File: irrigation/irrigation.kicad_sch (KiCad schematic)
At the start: 28 parts, among them J1 Power, J2 Power, J3 Power, J4 Power, J5 Power, J6 Power, J7 24V Jmp, J8 0V Jmp, K1 PLC-RPT-24DC/21, K3 PLC-RPT-24DC/21, M1 Pump, SW1 25% Full, SW2 50% Full, SW3 75% Full, SW4 100% Full, SW5 Well Empty, U1 MPPT-Charger

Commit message: More labels
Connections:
- net 8: now reaches K1.11, K3.14
- no-connect marks 0 -> 12
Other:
- note removed: "Need connectors for charge controller"
- moved on the sheet: BT1, BT2, SC1, SC2

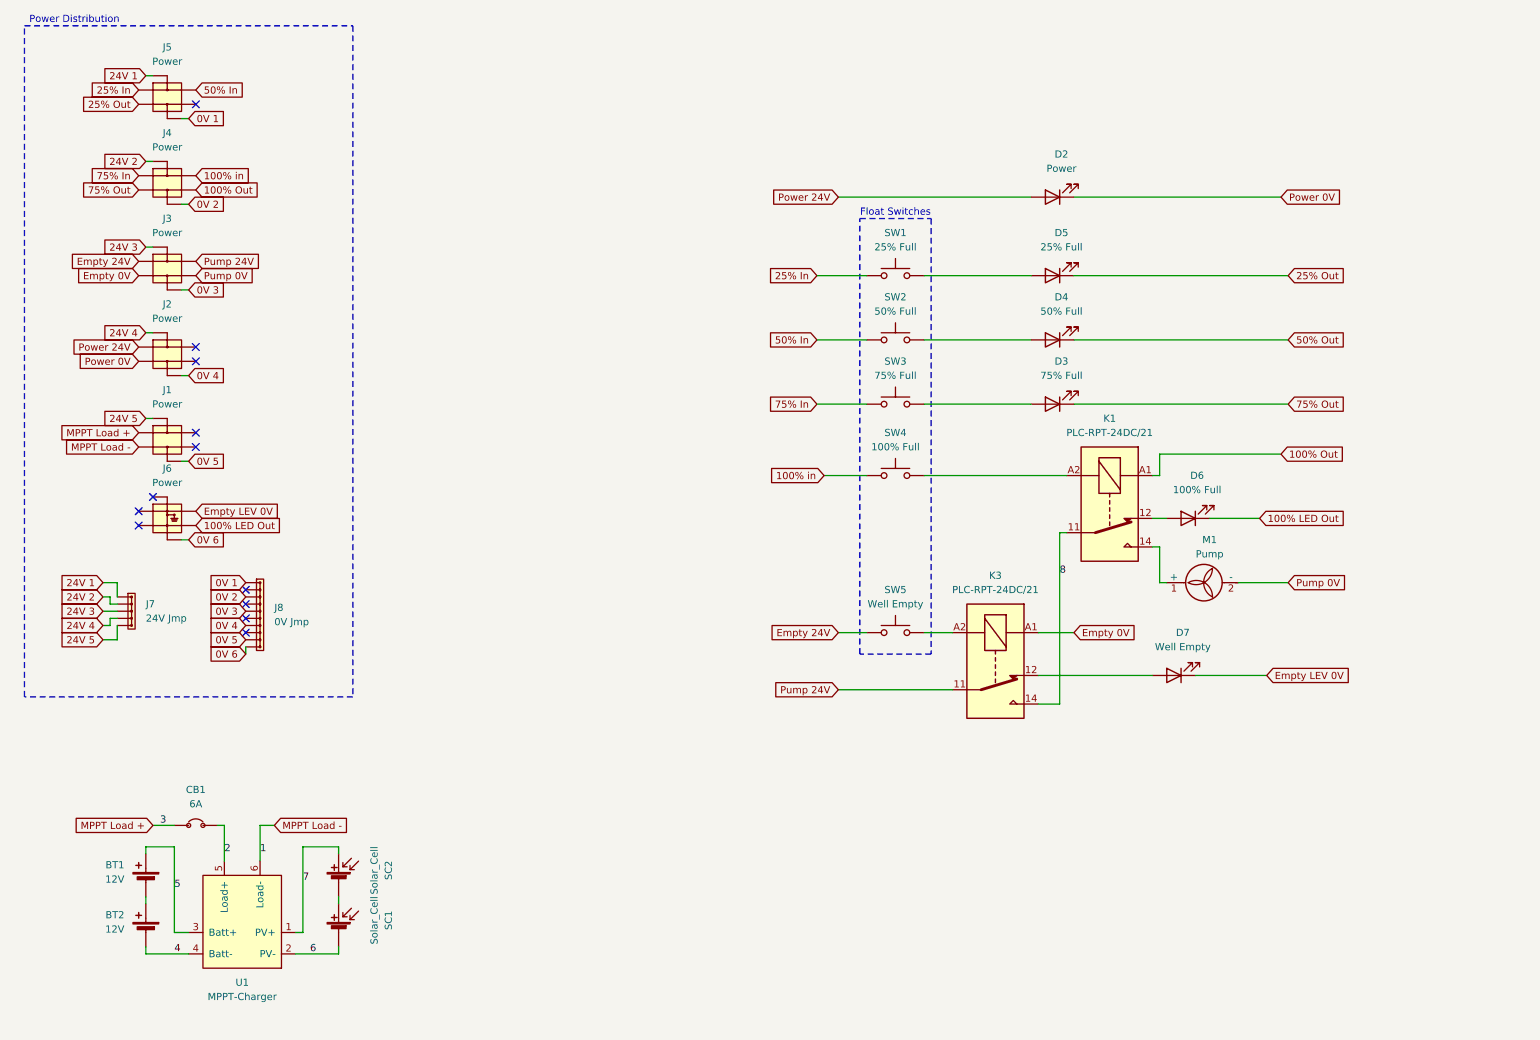
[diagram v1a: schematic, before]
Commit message: All wires labeled
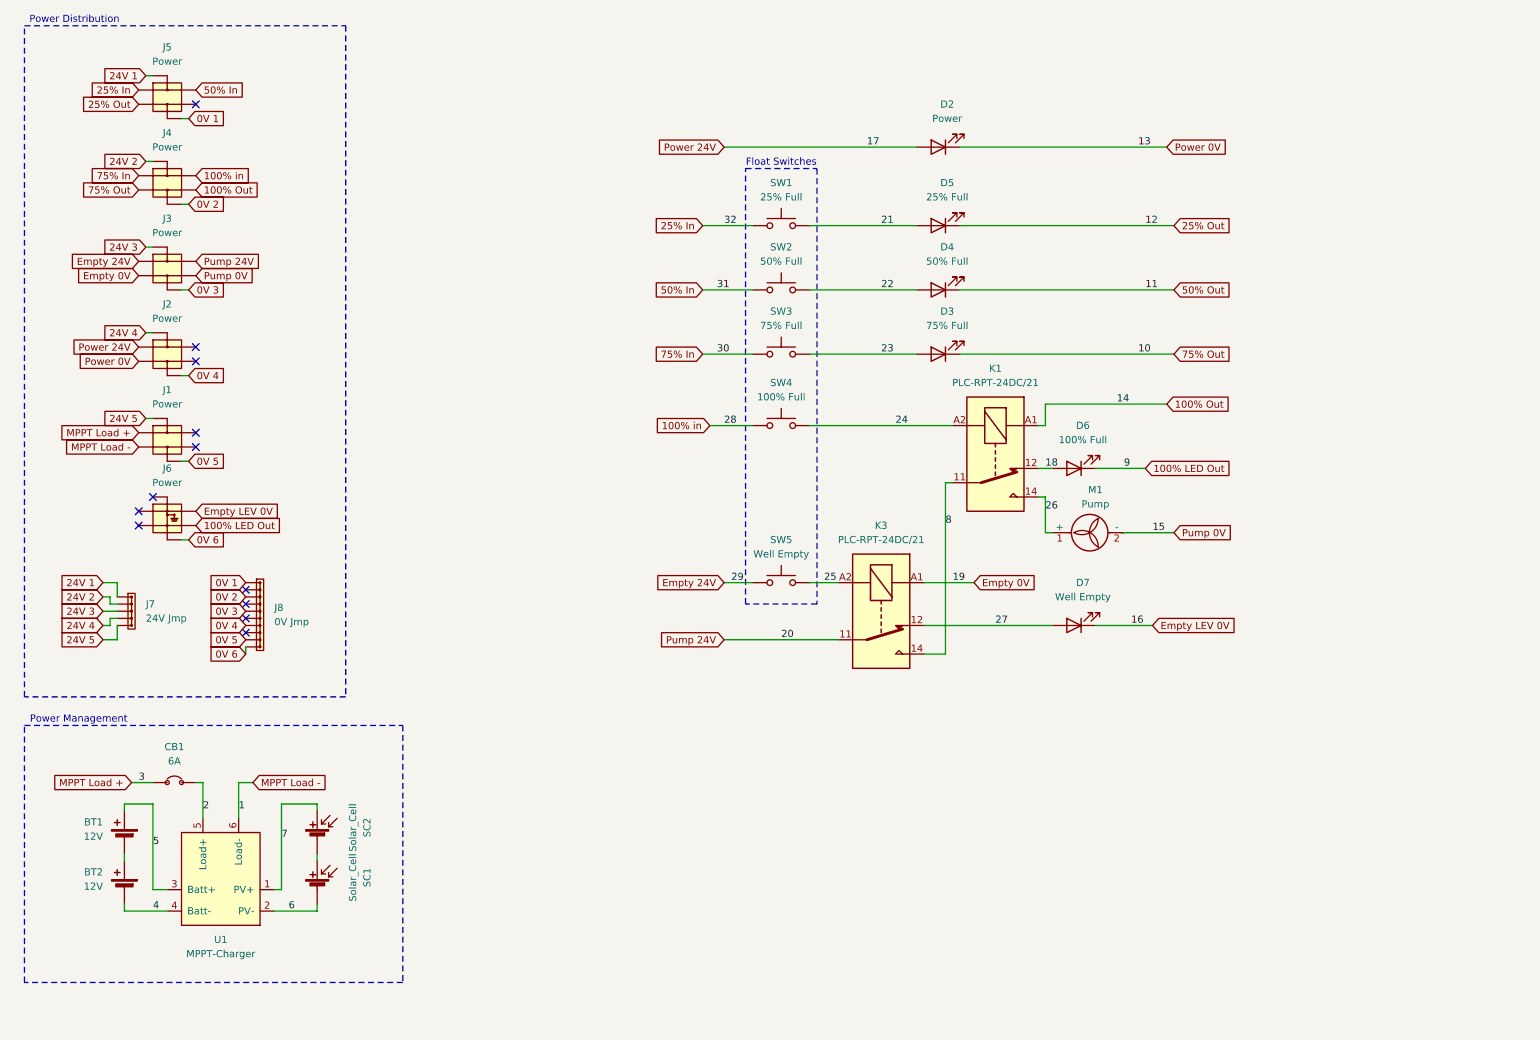
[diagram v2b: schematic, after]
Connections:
- net 23: now reaches D3.2 (A), SW3.2
- net 18: now reaches D6.2 (A), K1.12
- net 26: now reaches K1.14, M1.1 (+)
- net 25: now reaches K3.A2, SW5.2
- net 27: now reaches D7.2 (A), K3.12
- net 21: now reaches D5.2 (A), SW1.2
- net 22: now reaches D4.2 (A), SW2.2
- net 24: now reaches K1.A2, SW4.2
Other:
- note added: "Power Management"
- moved on the sheet: BT1, BT2, CB1, D2, D3, D4, D5, D6, D7, K1, K3, M1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

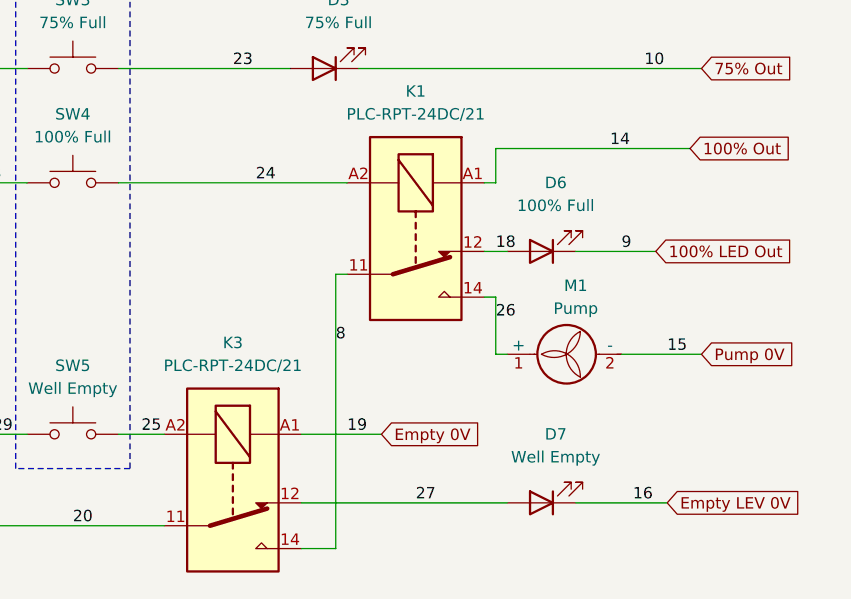
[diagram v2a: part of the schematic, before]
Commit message: Fixing schematic
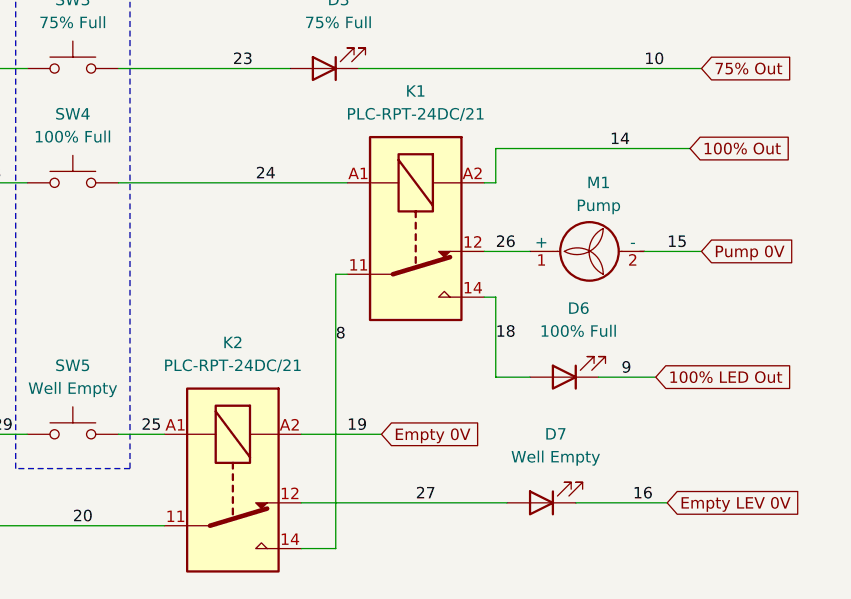
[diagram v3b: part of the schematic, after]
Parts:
- removed K1, K3: PLC-RPT-24DC/21, symbol Irrigation:PLC-RPT-24DC/21
- added K1, K2: PLC-RPT-24DC/21, symbol Phoenix Contact:PLC-RPT-24DC/21
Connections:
- net 100% Out: now also K1.A2
- net 18: now also K1.14
- net 24: now also K1.A1
- net 25: now also K2.A1
- net 26: now also K1.12
- net 27: now also K2.12
- net 8: now also K1.11, K2.14
- net Empty 0V: now also K2.A2
- net Pump 24V: now also K2.11
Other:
- moved on the sheet: D6, M1

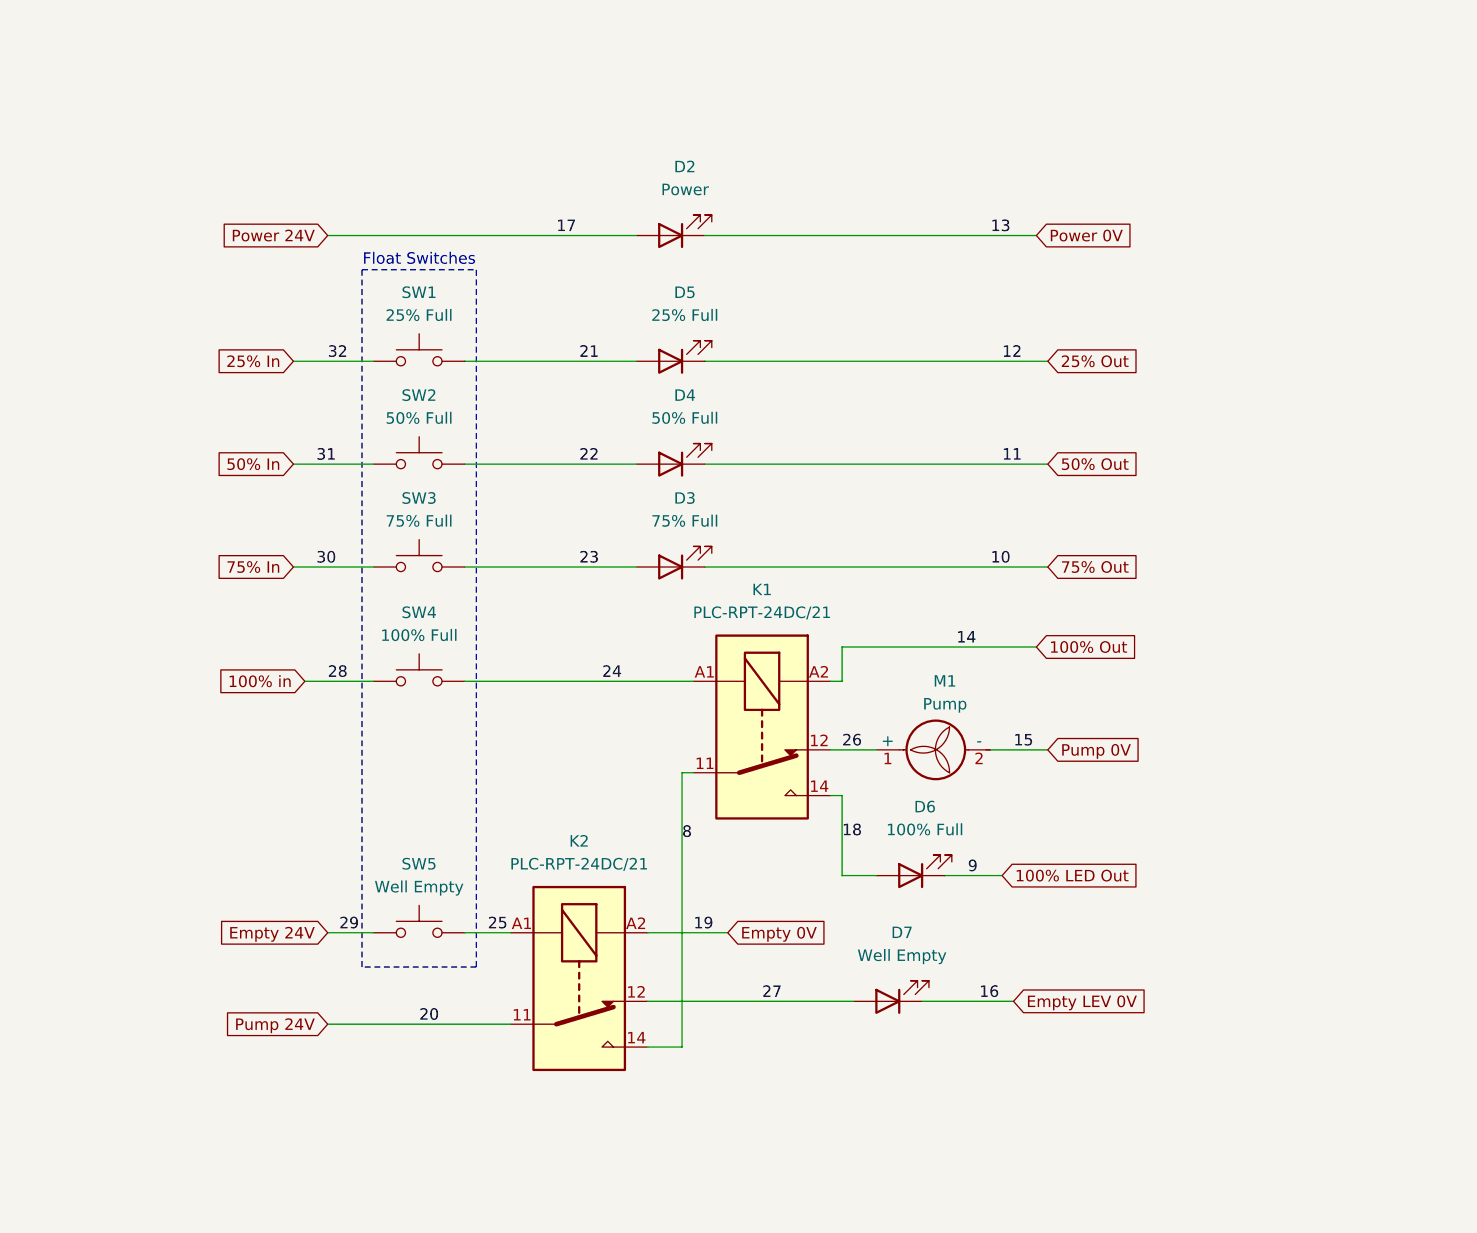
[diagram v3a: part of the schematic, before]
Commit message: Leaving a mess to remind me to update the schematic
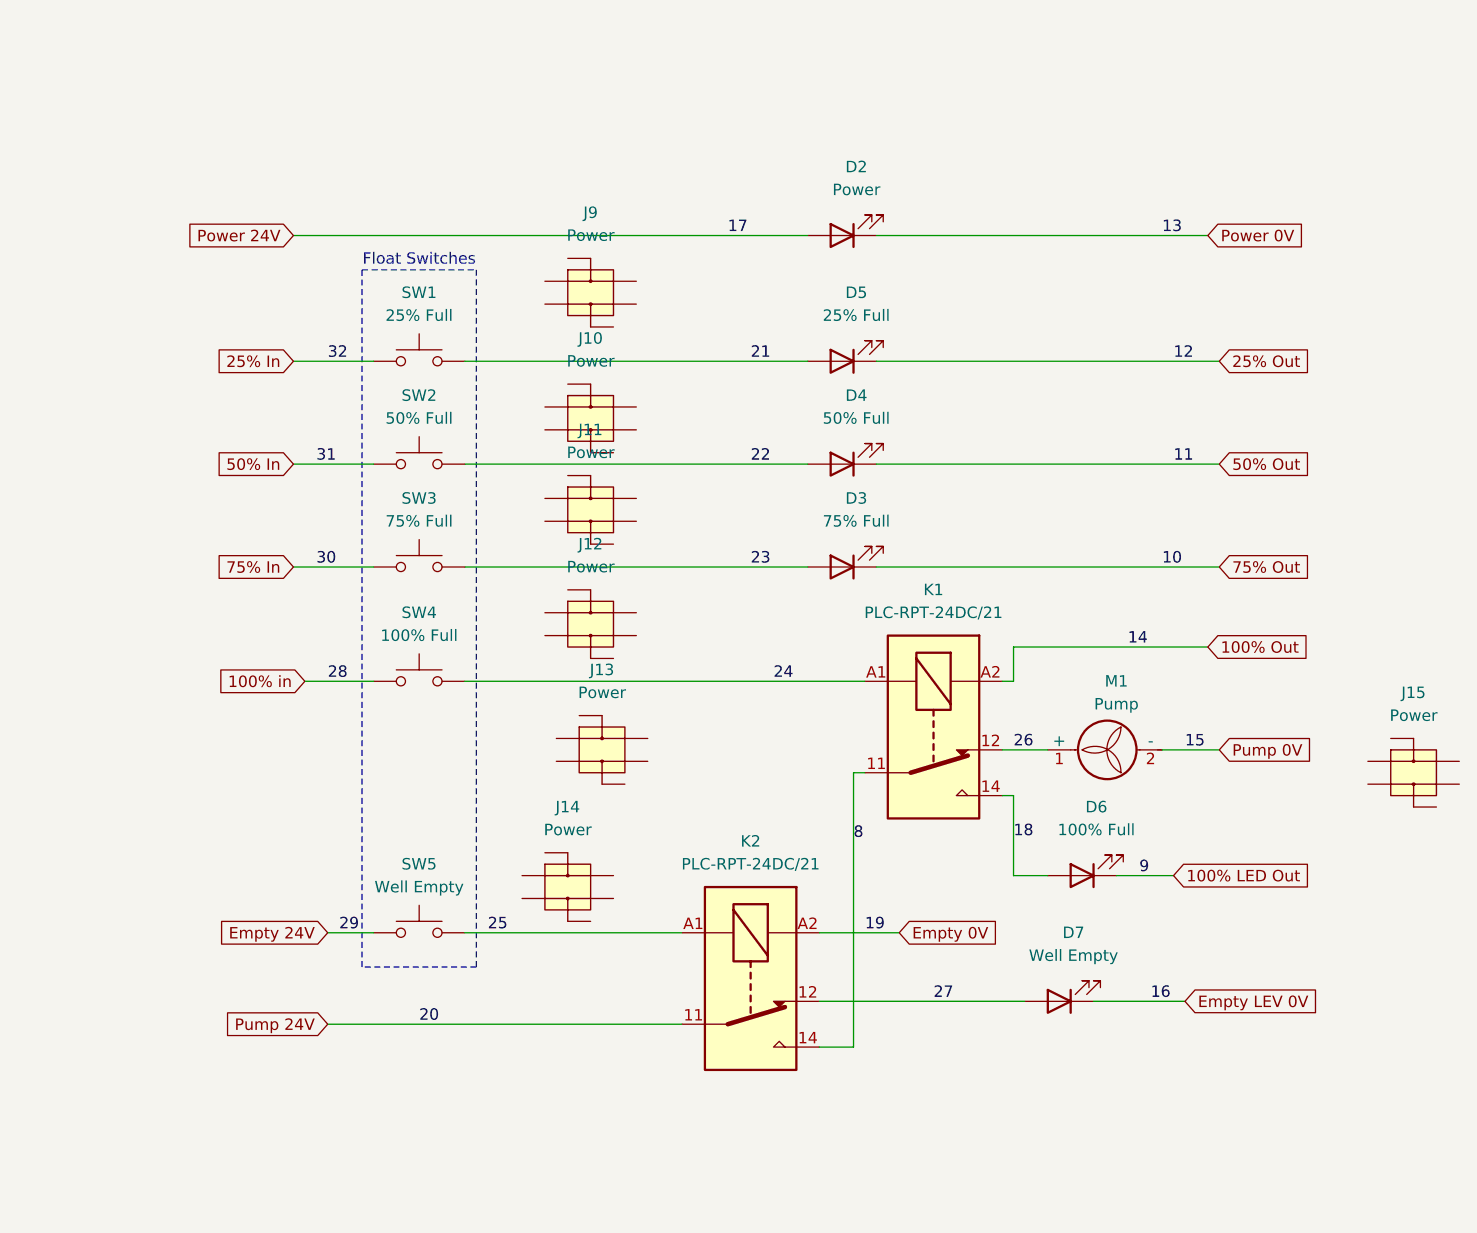
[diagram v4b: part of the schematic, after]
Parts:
- added J10, J11, J12, J13, J14, J15, J9: Power, symbol Phoenix Contact:PTTB_2,5-L/N_3210994
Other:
- moved on the sheet: D2, D3, D4, D5, D6, D7, K1, K2, M1
